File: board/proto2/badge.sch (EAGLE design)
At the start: 12 parts

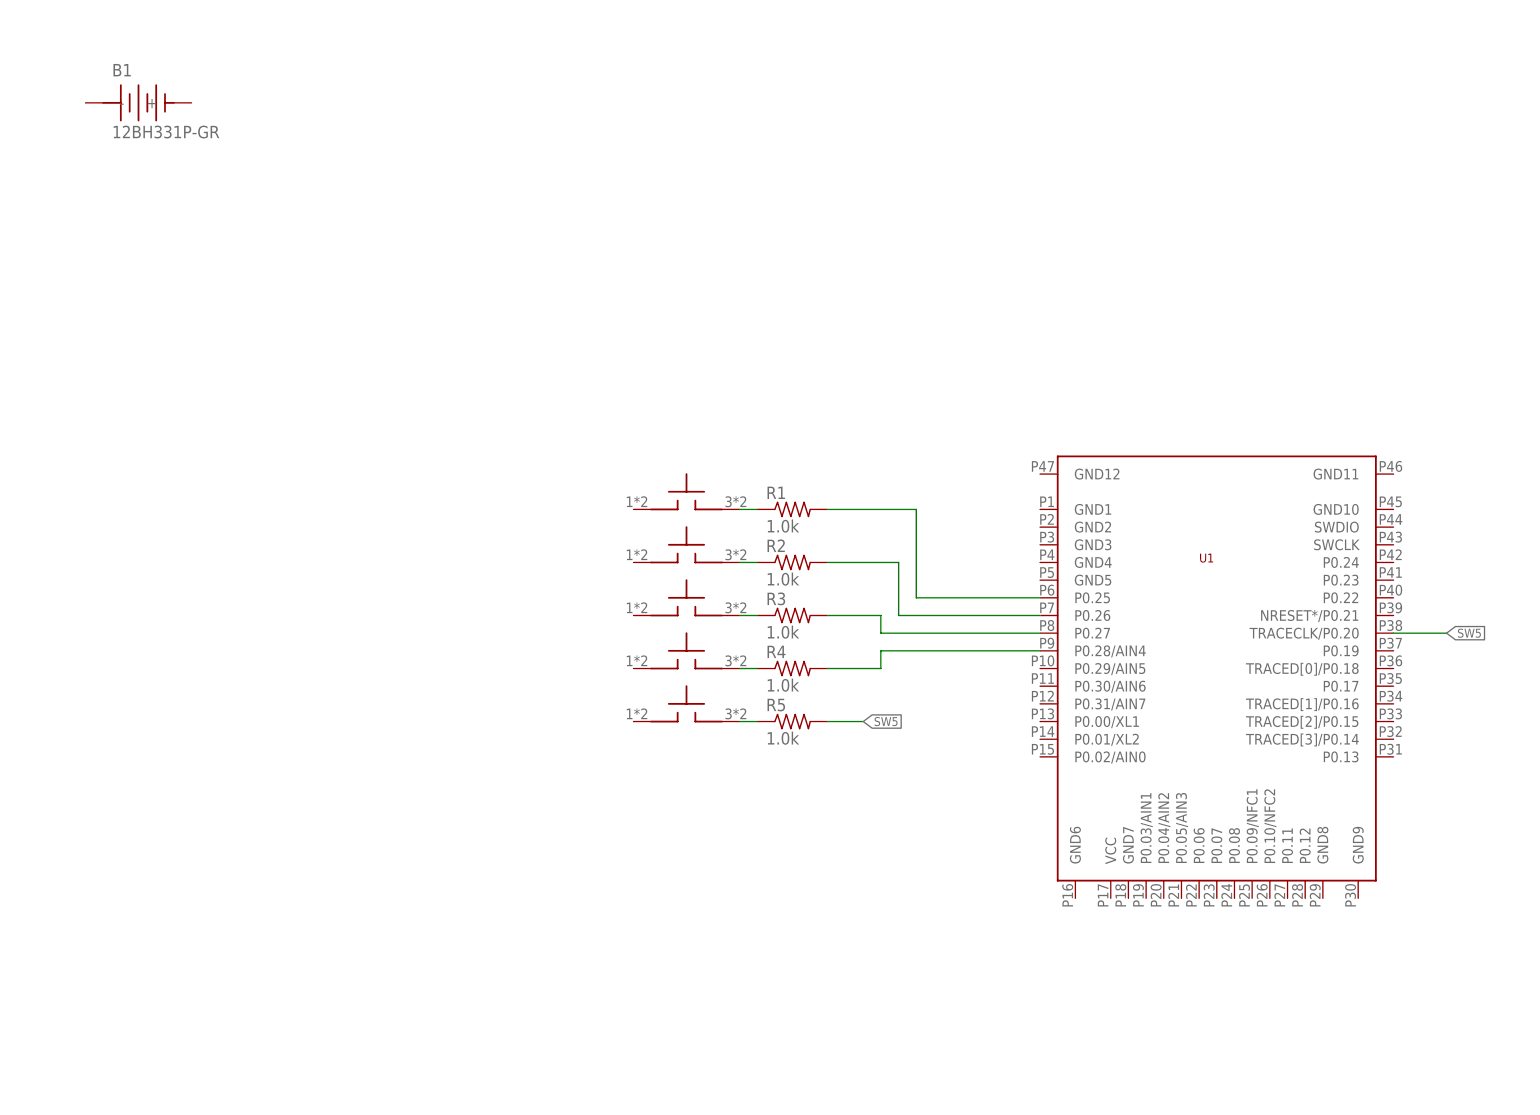
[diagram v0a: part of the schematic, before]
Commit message: added power suppy to proto2
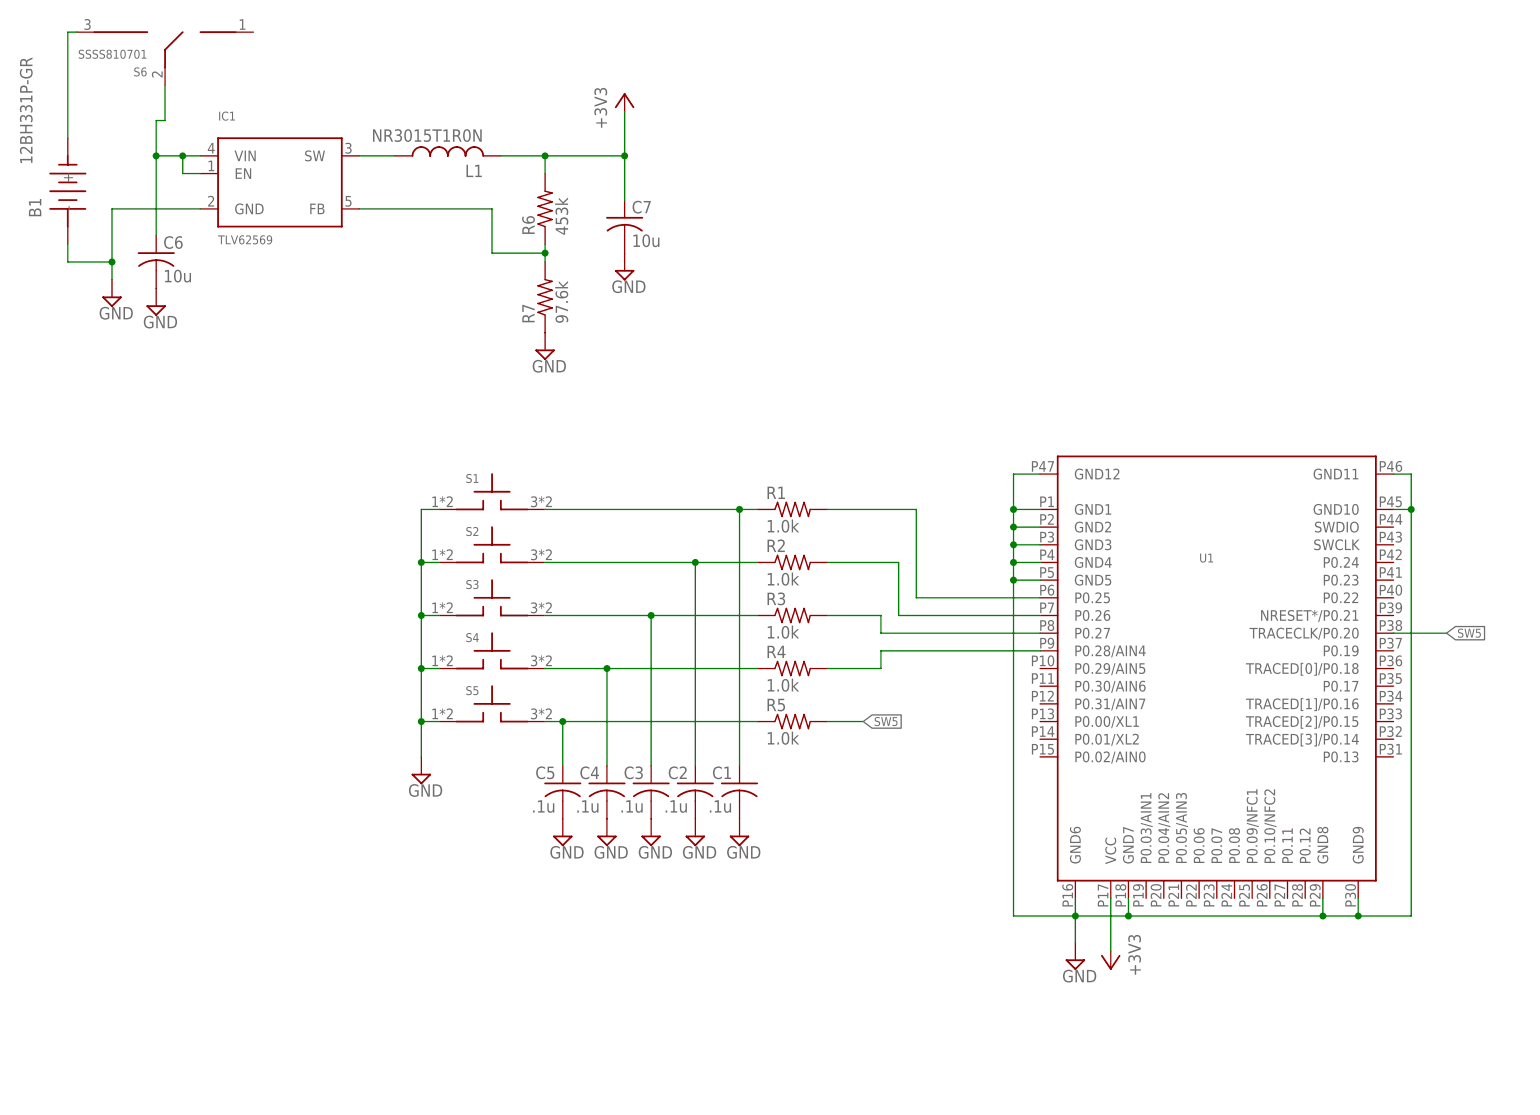
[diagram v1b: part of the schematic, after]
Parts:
- added C1, C2, C3, C4, C5: .1u, rcl:C-USC0201
- added C6, C7: 10u, rcl:C-USC0805K
- added IC1: TLV62569, badge:TLV62569
- added L1: NR3015T1R0N, badge:NR3015
- added R6: 453k, rcl:R-US_R0603
- added R7: 97.6k, rcl:R-US_R0603
- added S6: SSSS810701, badge:SSSS810701
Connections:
- new net +3V3: C7.1, L1.2, R6.2, U1.VCC
- new net GND: B1.-, C1.2, C2.2, C3.2, C4.2, C5.2, C6.2, C7.2, IC1.GND, R7.1, S1.A, S2.A, S3.A, S4.A, S5.A, U1.GND1, U1.GND10, U1.GND11, U1.GND12, U1.GND2, U1.GND3, U1.GND4, U1.GND5, U1.GND6, U1.GND7, U1.GND8, U1.GND9
- new net N$10: B1.+, S6.3
- new net N$11: C6.1, IC1.EN, IC1.VIN, S6.2
- new net N$12: IC1.FB, R6.1, R7.2
- new net N$14: IC1.SW, L1.1
- net N$1: now also C1.1
- net N$2: now also C2.1
- net N$3: now also C3.1
- net N$4: now also C4.1
- net N$5: now also C5.1
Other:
- note added: "ACTION"
- note added: "DOWN"
- note added: "LEFT"
- note added: "RIGHT"
- note added: "UP"
- moved on the sheet: B1

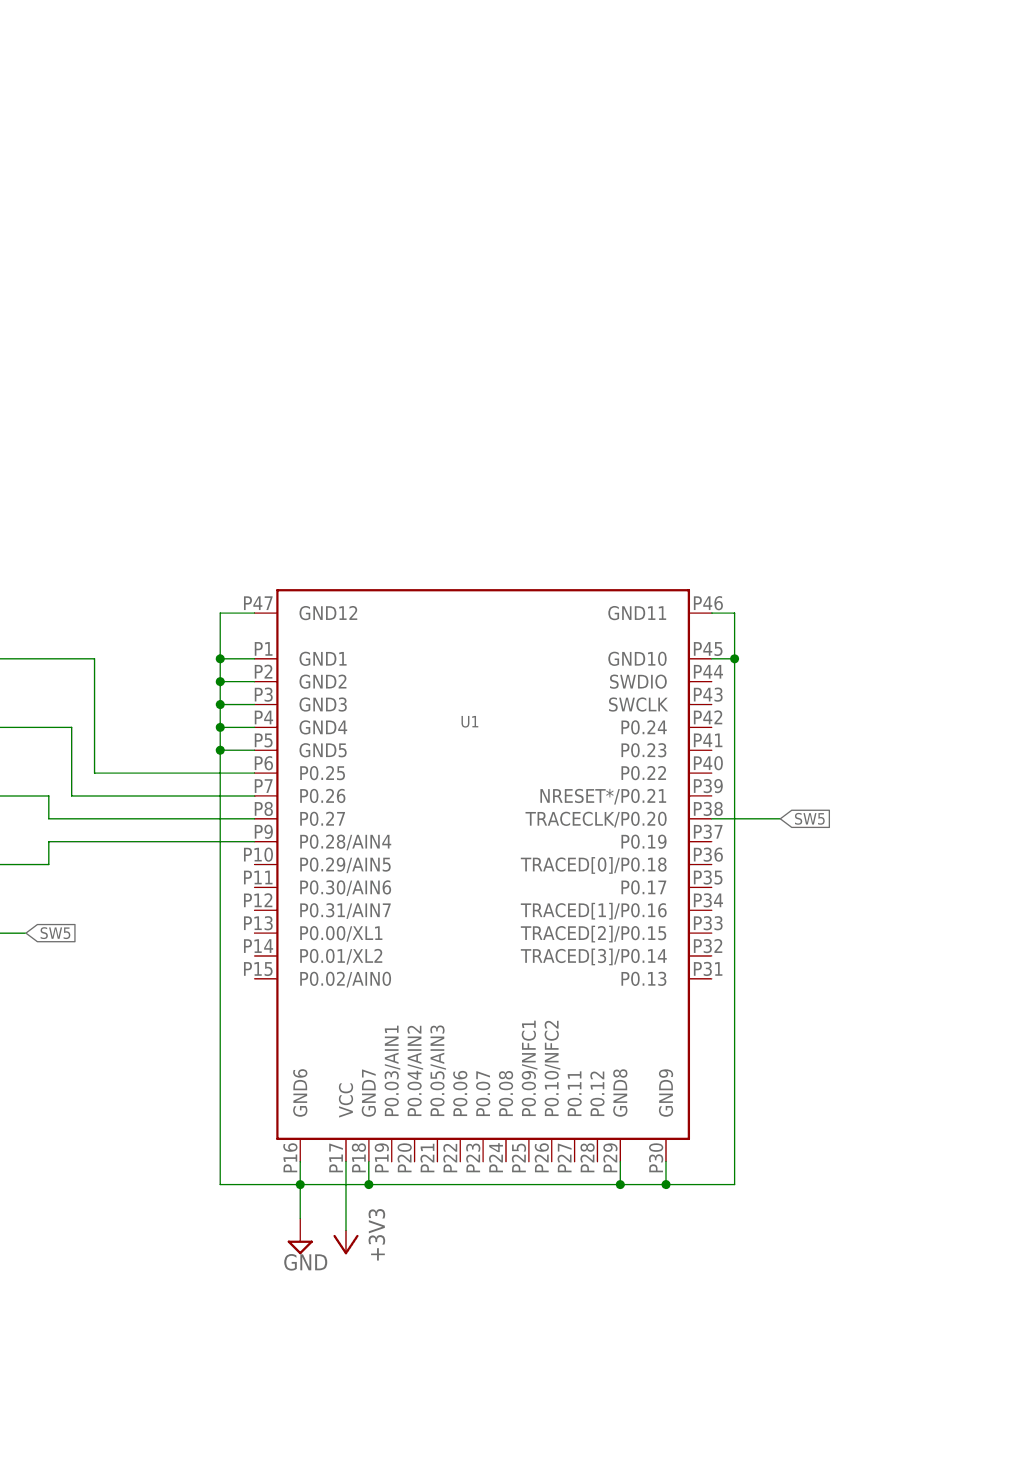
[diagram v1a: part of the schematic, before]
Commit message: adding additional parts
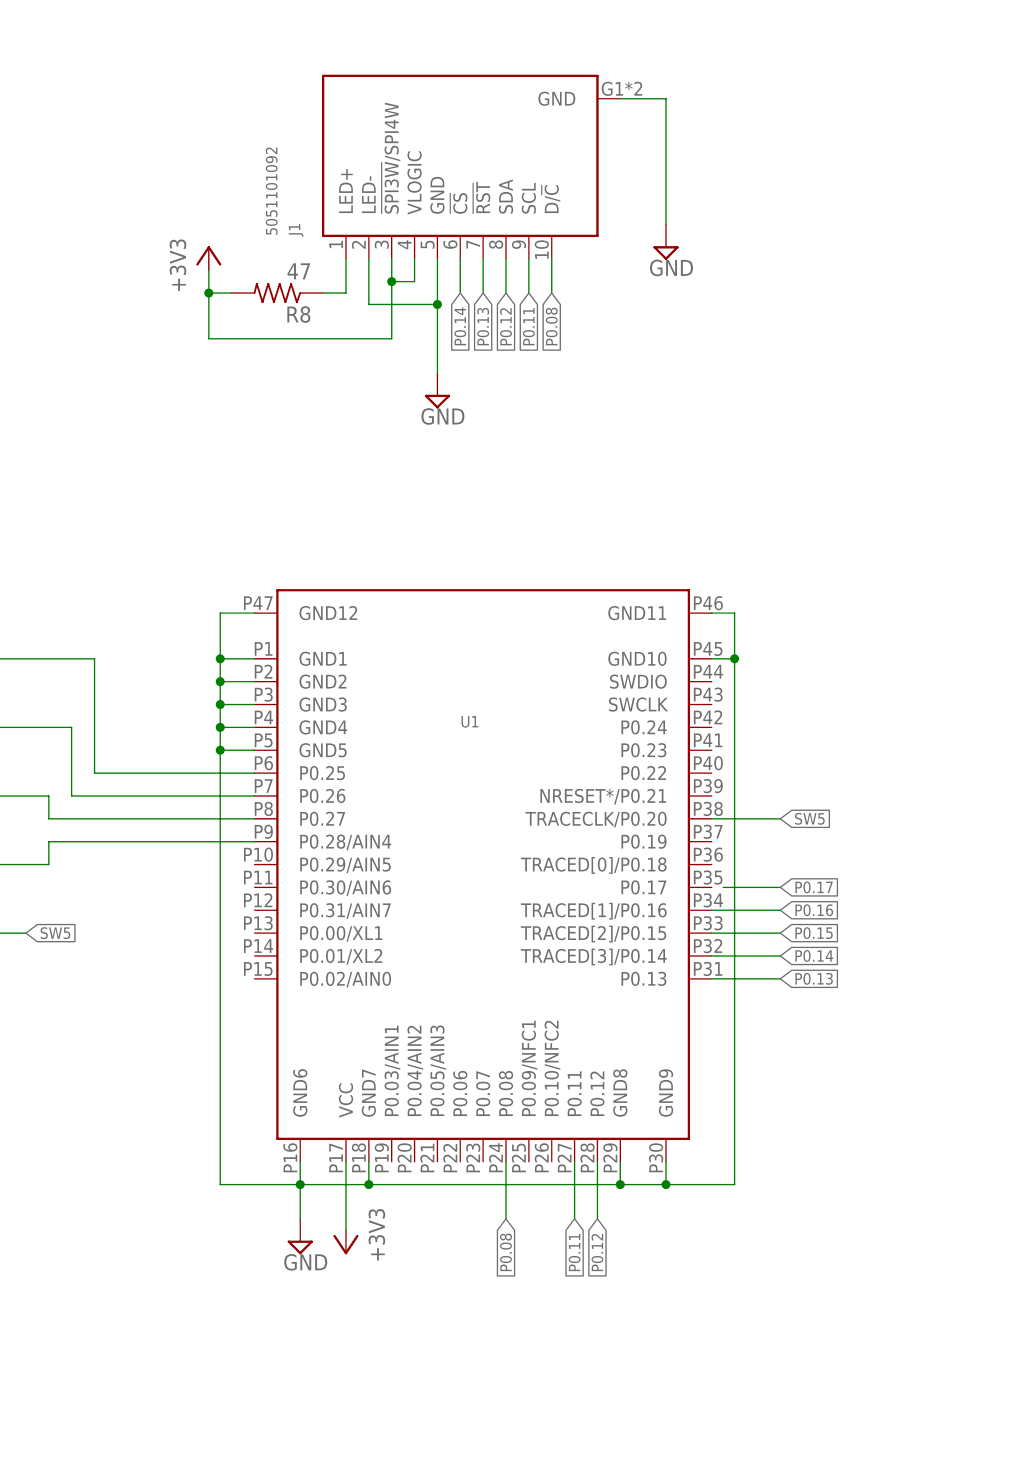
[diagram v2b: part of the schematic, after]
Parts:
- added J1: 5051101092, badge:5051101092
- added R8: 47, rcl:R-US_R0603
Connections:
- new net N$13: J1.LED+, R8.1
- new net P0.08: J1.D/!C, U1.P0.08
- new net P0.11: J1.SCL, U1.P0.11
- new net P0.12: J1.SDA, U1.P0.12
- new net P0.13: J1.!RST, U1.P0.13
- new net P0.14: J1.!CS, U1.TRACED[3]/P0.14
- new net P0.15: U1.TRACED[2]/P0.15
- new net P0.16: U1.TRACED[1]/P0.16
- net +3V3: now also J1.!SPI3W!/SPI4W, J1.VLOGIC, R8.2
- net GND: now also J1.GND, J1.GND@PADS, J1.LED-
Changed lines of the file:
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@@
 <part name="+3V1" library="supply1" deviceset="+3V3" device=""/>
 <part name="S6" library="badge" deviceset="SSSS810701" device=""/>
+<part name="SUPPLY12" library="supply2" deviceset="GND" device=""/>
+<part name="R8" library="rcl" deviceset="R-US_" device="R0603" value="47"/>
+<part name="+3V2" library="supply1" deviceset="+3V3" device=""/>
+<part name="SUPPLY13" library="supply2" deviceset="GND" device=""/>
+<part name="J1" library="badge" deviceset="5051101092" device=""/>
 </parts>
 <sheets>
@@
 <instance part="+3V1" gate="G$1" x="172.72" y="129.54" rot="R180"/>
 <instance part="S6" gate="G$1" x="36.83" y="264.16" rot="R180"/>
+<instance part="SUPPLY12" gate="GND" x="208.28" y="241.3"/>
+<instance part="R8" gate="G$1" x="165.1" y="236.22" rot="R180"/>
+<instance part="+3V2" gate="G$1" x="157.48" y="241.3"/>
+<instance part="SUPPLY13" gate="GND" x="182.88" y="224.79"/>
+<instance part="J1" gate="G$1" x="185.42" y="247.65" rot="R90"/>
 </instances>
 <busses>
@@
 <pinref part="SUPPLY11" gate="GND" pin="GND"/>
 </segment>
+<segment>
+<pinref part="SUPPLY12" gate="GND" pin="GND"/>
+<wire x1="208.28" y1="257.81" x2="208.28" y2="243.84" width="0.1524" layer="91"/>
+<pinref part="J1" gate="G$1" pin="GND@PADS"/>
+<wire x1="203.2" y1="257.81" x2="208.28" y2="257.81" width="0.1524" layer="91"/>
+</segment>
+<segment>
+<wire x1="175.26" y1="240.03" x2="175.26" y2="234.95" width="0.1524" layer="91"/>
+<wire x1="175.26" y1="234.95" x2="182.88" y2="234.95" width="0.1524" layer="91"/>
+<wire x1="182.88" y1="234.95" x2="182.88" y2="240.03" width="0.1524" layer="91"/>
+<wire x1="182.88" y1="234.95" x2="182.88" y2="227.33" width="0.1524" layer="91"/>
+<junction x="182.88" y="234.95"/>
+<pinref part="SUPPLY13" gate="GND" pin="GND"/>
+<pinref part="J1" gate="G$1" pin="LED-"/>
+<pinref part="J1" gate="G$1" pin="GND"/>
+</segment>
 </net>
 <net name="N$10" class="0">
@@
 <pinref part="+3V1" gate="G$1" pin="+3V3"/>
 </segment>
+<segment>
+<wire x1="177.8" y1="240.03" x2="177.8" y2="237.49" width="0.1524" layer="91"/>
+<wire x1="177.8" y1="237.49" x2="177.8" y2="231.14" width="0.1524" layer="91"/>
+<wire x1="177.8" y1="231.14" x2="157.48" y2="231.14" width="0.1524" layer="91"/>
+<wire x1="157.48" y1="231.14" x2="157.48" y2="236.22" width="0.1524" layer="91"/>
+<pinref part="R8" gate="G$1" pin="2"/>
+<wire x1="157.48" y1="236.22" x2="157.48" y2="238.76" width="0.1524" layer="91"/>
+<wire x1="160.02" y1="236.22" x2="157.48" y2="236.22" width="0.1524" layer="91"/>
+<junction x="157.48" y="236.22"/>
+<wire x1="180.34" y1="240.03" x2="180.34" y2="237.49" width="0.1524" layer="91"/>
+<wire x1="180.34" y1="237.49" x2="177.8" y2="237.49" width="0.1524" layer="91"/>
+<junction x="177.8" y="237.49"/>
+<pinref part="+3V2" gate="G$1" pin="+3V3"/>
+<pinref part="J1" gate="G$1" pin="!SPI3W!/SPI4W"/>
+<pinref part="J1" gate="G$1" pin="VLOGIC"/>
+</segment>
 </net>
 <net name="N$14" class="0">
@@
 </segment>
 </net>
+<net name="N$13" class="0">
+<segment>
+<wire x1="172.72" y1="240.03" x2="172.72" y2="236.22" width="0.1524" layer="91"/>
+<pinref part="R8" gate="G$1" pin="1"/>
+<wire x1="172.72" y1="236.22" x2="170.18" y2="236.22" width="0.1524" layer="91"/>
+<pinref part="J1" gate="G$1" pin="LED+"/>
+</segment>
+</net>
+<net name="P0.14" class="0">
+<segment>
+<pinref part="U1" gate="G$1" pin="TRACED[3]/P0.14"/>
+<wire x1="213.36" y1="162.56" x2="220.98" y2="162.56" width="0.1524" layer="91"/>
+<label x="220.98" y="162.56" size="1.27" layer="91" xref="yes"/>
+</segment>
+<segment>
+<wire x1="185.42" y1="240.03" x2="185.42" y2="236.22" width="0.1524" layer="91"/>
+<label x="185.42" y="236.22" size="1.27" layer="91" rot="R270" xref="yes"/>
+<pinref part="J1" gate="G$1" pin="!CS"/>
+</segment>
+</net>
+<net name="P0.15" class="0">
+<segment>
+<pinref part="U1" gate="G$1" pin="TRACED[2]/P0.15"/>
+<wire x1="213.36" y1="165.1" x2="220.98" y2="165.1" width="0.1524" layer="91"/>
+<label x="220.98" y="165.1" size="1.27" layer="91" xref="yes"/>
+</segment>
+</net>
+<net name="P0.16" class="0">
+<segment>
+<pinref part="U1" gate="G$1" pin="TRACED[1]/P0.16"/>
+<wire x1="213.36" y1="167.64" x2="220.98" y2="167.64" width="0.1524" layer="91"/>
+<label x="220.98" y="167.64" size="1.27" layer="91" xref="yes"/>
+</segment>
+</net>
+<net name="P0.17" class="0">
+<segment>
+<wire x1="214.63" y1="170.18" x2="220.98" y2="170.18" width="0.1524" layer="91"/>
+<label x="220.98" y="170.18" size="1.27" layer="91" xref="yes"/>
+</segment>
+</net>
+<net name="P0.11" class="0">
+<segment>
+<pinref part="U1" gate="G$1" pin="P0.11"/>
+<wire x1="198.12" y1="139.7" x2="198.12" y2="133.35" width="0.1524" layer="91"/>
+<label x="198.12" y="133.35" size="1.27" layer="91" rot="R270" xref="yes"/>
+</segment>
+<segment>
+<wire x1="193.04" y1="240.03" x2="193.04" y2="236.22" width="0.1524" layer="91"/>
+<label x="193.04" y="236.22" size="1.27" layer="91" rot="R270" xref="yes"/>
+<pinref part="J1" gate="G$1" pin="SCL"/>
+</segment>
+</net>
+<net name="P0.12" class="0">
+<segment>
+<pinref part="U1" gate="G$1" pin="P0.12"/>
+<wire x1="200.66" y1="139.7" x2="200.66" y2="133.35" width="0.1524" layer="91"/>
+<label x="200.66" y="133.35" size="1.27" layer="91" rot="R270" xref="yes"/>
+</segment>
+<segment>
+<wire x1="190.5" y1="240.03" x2="190.5" y2="236.22" width="0.1524" layer="91"/>
+<label x="190.5" y="236.22" size="1.27" layer="91" rot="R270" xref="yes"/>
+<pinref part="J1" gate="G$1" pin="SDA"/>
+</segment>
+</net>
+<net name="P0.13" class="0">
+<segment>
+<wire x1="187.96" y1="240.03" x2="187.96" y2="236.22" width="0.1524" layer="91"/>
+<label x="187.96" y="236.22" size="1.27" layer="91" rot="R270" xref="yes"/>
+<pinref part="J1" gate="G$1" pin="!RST"/>
+</segment>
+<segment>
+<pinref part="U1" gate="G$1" pin="P0.13"/>
+<wire x1="213.36" y1="160.02" x2="220.98" y2="160.02" width="0.1524" layer="91"/>
+<label x="220.98" y="160.02" size="1.27" layer="91" xref="yes"/>
+</segment>
+</net>
+<net name="P0.08" class="0">
+<segment>
+<wire x1="195.58" y1="240.03" x2="195.58" y2="236.22" width="0.1524" layer="91"/>
+<label x="195.58" y="236.22" size="1.27" layer="91" rot="R270" xref="yes"/>
+<pinref part="J1" gate="G$1" pin="D/!C"/>
+</segment>
+<segment>
+<pinref part="U1" gate="G$1" pin="P0.08"/>
+<wire x1="190.5" y1="139.7" x2="190.5" y2="133.35" width="0.1524" layer="91"/>
+<label x="190.5" y="133.35" size="1.27" layer="91" rot="R270" xref="yes"/>
+</segment>
+</net>

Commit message: adding bling LEDs to proto2
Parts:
- added C10, C11, C12, C13, C14, C15, C16, C17, C18, C19, C20, C21, C22, C23, C8, C9: .1u, rcl:C-USC0201
- added LED1, LED10, LED11, LED12, LED13, LED14, LED15, LED16, LED2, LED3, LED4, LED5, LED6, LED7, LED8, LED9: WS2812B, badge:WS2812B
- added R9: 47, rcl:R-US_R0603
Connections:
- new net N$15: LED5.DOUT, LED6.DIN
- new net N$16: LED10.DIN, LED9.DOUT
- new net N$17: LED13.DOUT, LED14.DIN
- new net N$18: LED1.DOUT, LED2.DIN
- new net N$19: LED6.DOUT, LED7.DIN
- new net N$20: LED10.DOUT, LED11.DIN
- new net N$21: LED14.DOUT, LED15.DIN
- new net N$22: LED3.DOUT, LED4.DIN
- new net N$23: LED7.DOUT, LED8.DIN
- new net N$24: LED2.DOUT, LED3.DIN
- new net N$25: LED11.DOUT, LED12.DIN
- new net N$26: LED15.DOUT, LED16.DIN
- new net N$27: LED4.DOUT, LED5.DIN
- new net N$28: LED8.DOUT, LED9.DIN
- new net N$29: LED12.DOUT, LED13.DIN
- new net N$30: LED1.DIN, R9.1
- new net P0.02: R9.2, U1.P0.02/AIN0
- net +3V3: now also C10.1, C11.1, C12.1, C13.1, C14.1, C15.1, C16.1, C17.1, C18.1, C19.1, C20.1, C21.1, C22.1, C23.1, C8.1, C9.1, LED1.VDD, LED10.VDD, LED11.VDD, LED12.VDD, LED13.VDD, LED14.VDD, LED15.VDD, LED16.VDD, LED2.VDD, LED3.VDD, LED4.VDD, LED5.VDD, LED6.VDD, LED7.VDD, LED8.VDD, LED9.VDD
- net GND: now also C10.2, C11.2, C12.2, C13.2, C14.2, C15.2, C16.2, C17.2, C18.2, C19.2, C20.2, C21.2, C22.2, C23.2, C8.2, C9.2, LED1.VSS, LED10.VSS, LED11.VSS, LED12.VSS, LED13.VSS, LED14.VSS, LED15.VSS, LED16.VSS, LED2.VSS, LED3.VSS, LED4.VSS, LED5.VSS, LED6.VSS, LED7.VSS, LED8.VSS, LED9.VSS
